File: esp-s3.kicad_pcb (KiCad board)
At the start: 2 copper layers, 12 parts, among them U1 ESP32-S3, U2 W25Q16JVSS

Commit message: 🚀初步完善原理图
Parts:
- added AE2: Antenna_Shield, RF_Antenna:Texas_SWRA117D_2.4GHz_Left, F.Cu at (175.7, 86.2)
- added C10: 10pf, Capacitor_SMD:C_0402_1005Metric, F.Cu at (99.9, 105.7)
- added C11: 10pf, Capacitor_SMD:C_0402_1005Metric, F.Cu at (99.9, 107.7)
- added C12: 1uf, Capacitor_SMD:C_0402_1005Metric, F.Cu at (99.9, 109.6)
- added C13: 10uf, Capacitor_SMD:C_0402_1005Metric, F.Cu at (99.9, 111.6)
- added C14: 1uf, Capacitor_SMD:C_0402_1005Metric, F.Cu at (99.9, 113.6)
- added C15: 10uf, Capacitor_SMD:C_0402_1005Metric, F.Cu at (102.8, 105.7)
- added C16: 100nf, Capacitor_SMD:C_0402_1005Metric, F.Cu at (102.8, 107.7)
- added C17: 1uf, Capacitor_SMD:C_0402_1005Metric, F.Cu at (102.8, 109.6)
- added C18: 15pf, Capacitor_SMD:C_0402_1005Metric, F.Cu at (102.8, 111.6)
- added C19: 15pf, Capacitor_SMD:C_0402_1005Metric, F.Cu at (102.8, 113.6)
- added C20: 4.7PF, Capacitor_SMD:C_0402_1005Metric, F.Cu at (160.5, 86.5)
- added C21: 2.4pf, Capacitor_SMD:C_0402_1005Metric, F.Cu at (159.8, 88.9)
- added D1: NCD0603R1, LED_SMD:LED_0603_1608Metric, F.Cu at (109.6, 96.5)
- added D2: NCD0603R1, LED_SMD:LED_0603_1608Metric, F.Cu at (144.5, 101.6)
- added J1: USB1, Connector_USB:USB_C_Receptacle_G-Switch_GT-USB-7010ASV, F.Cu at (179.6, 133.2)
- added J2: USB1, Connector_USB:USB_C_Receptacle_G-Switch_GT-USB-7010ASV, F.Cu at (165.9, 132.4)
- added L2: 2.4nh, Inductor_SMD:L_0402_1005Metric, F.Cu at (162.6, 90.6)
- added R1: 100Ω, Resistor_SMD:R_0402_1005Metric, F.Cu at (99.9, 91.8)
- added R2: 4.7kΩ, Resistor_SMD:R_0402_1005Metric, F.Cu at (99.9, 93.8)
- added R3: 5.1K, Resistor_SMD:R_0402_1005Metric, F.Cu at (99.9, 95.8)
- added R4: 4.7kΩ, Resistor_SMD:R_0402_1005Metric, F.Cu at (99.9, 97.8)
- added R5: 5.1K, Resistor_SMD:R_0402_1005Metric, F.Cu at (99.9, 99.7)
- added R6: 5.1K, Resistor_SMD:R_0402_1005Metric, F.Cu at (99.9, 101.7)
- added R7: 5.1K, Resistor_SMD:R_0402_1005Metric, F.Cu at (99.9, 103.7)
- added R8: 100Ω, Resistor_SMD:R_0402_1005Metric, F.Cu at (143.9, 103.8)
- added SW1: SW_Push, SmartLock:SW-SMD_L3.9-W3.0-P4.45, F.Cu at (107.5, 106.8)
- added SW3: SW_Push, SmartLock:SW-SMD_L3.9-W3.0-P4.45, F.Cu at (107.5, 111.1)
- added U3: ME6231A33PG, Package_TO_SOT_SMD:SOT-89-3, F.Cu at (104.8, 98.3)
- added U4: CH343P, Package_DFN_QFN:WCH_QFN-16-1EP_3x3mm_P0.5mm_EP1.8x1.8mm, F.Cu at (89.4, 113.6)
- added Y1: Crystal_GND24, Crystal:Crystal_SMD_3225-4Pin_3.2x2.5mm, F.Cu at (178.7, 101.3)
- added Y2: Crystal, SmartLock:Crystal_SMD_ECS_CSM3X-2Pin_7.5x3.1mm, F.Cu at (164.8, 108.3)
- moved U2 55.8 mm to (176.9, 111.0)
- moved U1 51.2 mm to (170.6, 97.9), turned to -90 degrees
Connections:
- C1 pad 1: VDD33 -> VDDSPI
- C2 pad 1: VDD33 -> VDDSPI
- C4 pad 1: VDD33 -> VDDSPI
- C5 pad 1: VDD33 -> VDDSPI
- C6 pad 1: VDD33 -> VDDSPI
- C7 pad 1: VDD33 -> VDDSPI
- C8 pad 1: VDD33 -> VDDSPI
- C9 pad 1: VDD33 -> VDDSPI
- L1 pad 2: VDD33 -> VDDSPI
- U1 pad 1: unconnected-(U1-LNA_IN-Pad1) -> LNA_IN
- U1 pad 10: unconnected-(U1-GPIO5-Pad10) -> GPIO5
- U1 pad 11: unconnected-(U1-GPIO6-Pad11) -> GPIO6
- U1 pad 12: unconnected-(U1-GPIO7-Pad12) -> GPIO7
- U1 pad 13: unconnected-(U1-GPIO8-Pad13) -> GPIO8
- U1 pad 14: unconnected-(U1-GPIO9-Pad14) -> GPIO9
- U1 pad 15: unconnected-(U1-GPIO10-Pad15) -> GPIO10
- U1 pad 16: unconnected-(U1-GPIO11-Pad16) -> GPIO11
- U1 pad 17: unconnected-(U1-GPIO12-Pad17) -> GPIO12
- U1 pad 18: unconnected-(U1-GPIO13-Pad18) -> GPIO13
- U1 pad 19: unconnected-(U1-GPIO14-Pad19) -> GPIO14
- U1 pad 21: unconnected-(U1-XTAL_32K_P-Pad21) -> RTC_P
- U1 pad 22: unconnected-(U1-XTAL_32K_N-Pad22) -> RTC_N
- U1 pad 23: unconnected-(U1-GPIO17-Pad23) -> GPIO17
- U1 pad 24: unconnected-(U1-GPIO18-Pad24) -> GPIO18
- U1 pad 25: unconnected-(U1-GPIO19/USB_D--Pad25) -> USB_D-
- U1 pad 26: unconnected-(U1-GPIO20/USB_D+-Pad26) -> USB_D+
- U1 pad 27: unconnected-(U1-GPIO21-Pad27) -> GPIO21
- U1 pad 29: VDD33 -> VDDSPI
- U1 pad 30: unconnected-(U1-SPIHD-Pad30) -> SPIHD
- U1 pad 31: unconnected-(U1-SPIWP-Pad31) -> SPIWP
- U1 pad 33: unconnected-(U1-SPICLK-Pad33) -> SPICLK
- U1 pad 34: unconnected-(U1-SPIQ-Pad34) -> SPIQ
- U1 pad 35: unconnected-(U1-SPID-Pad35) -> SPID
- U1 pad 36: unconnected-(U1-SPICLK_N-Pad36) -> GPIO48
- U1 pad 37: unconnected-(U1-SPICLK_P-Pad37) -> GPIO47
- U1 pad 38: unconnected-(U1-GPIO33-Pad38) -> GPIO33
- U1 pad 39: unconnected-(U1-GPIO34-Pad39) -> GPIO34
- U1 pad 4: unconnected-(U1-CHIP_PU-Pad4) -> CHIP_PU
- U1 pad 40: unconnected-(U1-GPIO35-Pad40) -> GPIO35
- U1 pad 41: unconnected-(U1-GPIO36-Pad41) -> GPIO36
- U1 pad 42: unconnected-(U1-GPIO37-Pad42) -> GPIO37
- U1 pad 43: unconnected-(U1-GPIO38-Pad43) -> GPIO38
- U1 pad 44: unconnected-(U1-MTCK-Pad44) -> GPIO39
- U1 pad 45: unconnected-(U1-MTDO-Pad45) -> GPIO40
- U1 pad 46: VDD33 -> VDDSPI
- U1 pad 47: unconnected-(U1-MTDI-Pad47) -> GPIO41
- U1 pad 48: unconnected-(U1-MTMS-Pad48) -> GPIO42
- U1 pad 49: unconnected-(U1-U0TXD-Pad49) -> TXD
- U1 pad 5: unconnected-(U1-GPIO0-Pad5) -> GPIO0
- U1 pad 50: unconnected-(U1-U0RXD-Pad50) -> RXD
- U1 pad 51: unconnected-(U1-GPIO45-Pad51) -> GPIO45
- U1 pad 52: unconnected-(U1-GPIO46-Pad52) -> GPIO46
- U1 pad 53: unconnected-(U1-XTAL_N-Pad53) -> XTAL_N
- U1 pad 54: unconnected-(U1-XTAL_P-Pad54) -> XTAL_P
- U1 pad 55: VDD33 -> VDDSPI
- U1 pad 56: VDD33 -> VDDSPI
- U1 pad 6: unconnected-(U1-GPIO1-Pad6) -> GPIO1
- U1 pad 7: unconnected-(U1-GPIO2-Pad7) -> GPIO2
- U1 pad 8: unconnected-(U1-GPIO3-Pad8) -> GPIO3
- U1 pad 9: unconnected-(U1-GPIO4-Pad9) -> GPIO4
- U2 pad 2: unconnected-(U2-DO/IO_{1}-Pad2) -> SPIQ
- U2 pad 3: unconnected-(U2-~{WP}/IO_{2}-Pad3) -> SPIWP
- U2 pad 4: unconnected-(U2-GND-Pad4) -> GND
- U2 pad 5: unconnected-(U2-DI/IO_{0}-Pad5) -> SPID
- U2 pad 6: unconnected-(U2-CLK-Pad6) -> SPICLK
- U2 pad 7: unconnected-(U2-~{HOLD}/~{RESET}/IO_{3}-Pad7) -> SPIHD
- U2 pad 8: unconnected-(U2-VCC-Pad8) -> VDDSPI
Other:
- board outline added: 30.7 x 56.6 mm

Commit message: 初步完成PCB
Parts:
- removed C18, C19: 15pf, Capacitor_SMD:C_0402_1005Metric
- removed Y2: Crystal, SmartLock:Crystal_SMD_ECS_CSM3X-2Pin_7.5x3.1mm
- added C22: 100nf, Capacitor_SMD:C_0402_1005Metric, F.Cu at (166.9, 94.3)
- added J3: Conn_01x15_Pin, Connector_PinHeader_2.54mm:PinHeader_1x20_P2.54mm_Vertical, F.Cu at (156.6, 80.3)
- added J4: Conn_01x15_Pin, Connector_PinHeader_2.54mm:PinHeader_1x20_P2.54mm_Vertical, F.Cu at (185.6, 80.0)
- SW1, SW3: footprint SmartLock:SW-SMD_L3.9-W3.0-P4.45 -> smartlock:SW-SMD_L3.9-W3.0-P4.45
- moved U4 88.4 mm to (177.8, 115.4)
- moved R5 82.5 mm to (180.1, 119.1), turned to -90 degrees
- moved R1 82.2 mm to (179.7, 111.5)
- moved R3 80.3 mm to (176.8, 118.9)
- moved C11 78.5 mm to (177.4, 95.0), turned to -90 degrees
- moved C10 78.5 mm to (177.4, 93.2), turned to 90 degrees
- moved C16 74.7 mm to (176.8, 118.0)
- moved C17 72.7 mm to (175.4, 113.3), turned to -90 degrees
- moved C14 72.7 mm to (168.2, 88.6), turned to 90 degrees
- moved C15 72.5 mm to (174.2, 118.1), turned to -90 degrees
- moved D1 71.4 mm to (179.7, 109.5), turned to -90 degrees
- moved C13 71.3 mm to (170.9, 118.5), turned to 180 degrees
- moved R7 70.1 mm to (168.3, 119.0), turned to -90 degrees
- moved C12 70.0 mm to (166.8, 88.7), turned to 90 degrees
- moved U3 68.6 mm to (171.2, 115.2), turned to 90 degrees
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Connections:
- C1 pad 1: VDDSPI -> VDD33
- C12 pad 1: Net-(C12-Pad1) -> GPIO0
- C14 pad 1: Net-(C14-Pad1) -> CHIP_PU
- C15 pad 1: VDDSPI -> VDD33
- C17 pad 2: VDDSPI -> VDD33
- C2 pad 1: VDDSPI -> VDD33
- C4 pad 1: VDDSPI -> VDD33
- C5 pad 1: VDDSPI -> VDD33
- C6 pad 1: VDDSPI -> VDD33
- C7 pad 1: VDDSPI -> VDD33
- D1 pad 1: GPIO2 -> GPIO39
- L1 pad 2: VDDSPI -> VDD33
- R1 pad 1: VDDSPI -> VDD33
- R2 pad 1: Net-(C12-Pad1) -> GPIO0
- R2 pad 2: VDDSPI -> VDD33
- R4 pad 1: Net-(C14-Pad1) -> CHIP_PU
- R4 pad 2: VDDSPI -> VDD33
- R8 pad 1: VDDSPI -> VDD33
- SW1 pad 1: Net-(C12-Pad1) -> GND
- SW3 pad 1: Net-(C14-Pad1) -> GND
- U1 pad 20: unconnected-(U1-VDD3P3_RTC-Pad20) -> VDD33
- U1 pad 21: RTC_P -> GPIO15
- U1 pad 22: RTC_N -> GPIO16
- U1 pad 46: VDDSPI -> VDD33
- U1 pad 55: VDDSPI -> VDD33
- U1 pad 56: VDDSPI -> VDD33
- U3 pad 3: VDDSPI -> VDD33
- U4 pad 1: VDDSPI -> VDD33
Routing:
- net VDD33: track 0.00 -> 132.3 mm, vias 0 -> 10
- net CHIP_PU: track 0.00 -> 62.3 mm, vias 0 -> 5
- net GPIO0: track 0.00 -> 58.6 mm, vias 0 -> 5
- net VBUS: track 0.00 -> 39.7 mm, vias 0 -> 6
- net GPIO18: track 0.00 -> 39.5 mm, vias 0 -> 2
- net GPIO48: track 0.00 -> 39.1 mm, vias 0 -> 1
- net GPIO21: track 0.00 -> 38.4 mm, vias 0 -> 1
- net GPIO47: track 0.00 -> 36.7 mm, vias 0 -> 1
- net GPIO17: track 0.00 -> 36.5 mm
- net GPIO16: track 0.00 -> 34.4 mm
- net GPIO33: track 0.00 -> 34.4 mm, vias 0 -> 1
- net USB_D-: track 0.00 -> 31.9 mm
- net GPIO39: track 0.00 -> 31.6 mm, vias 0 -> 2
- net GPIO34: track 0.00 -> 31.5 mm, vias 0 -> 1
- net GPIO15: track 0.00 -> 31.5 mm
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- added copper zone on B.Cu, net GND
- added copper zone on F.Cu, net GND
- added copper zone on In1.Cu, net GND
- added copper zone on In2.Cu, net GND
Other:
- board size 30.7 x 56.6 mm -> 32.4 x 51.6 mm
- copper layers 2 -> 4

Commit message: 添加pcb丝印
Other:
- board text added: "GND"
- board text added: "GPIO1"
- board text added: "GPIO10"
- board text added: "GPIO11"
- board text added: "GPIO12"
- board text added: "GPIO13"
- board text added: "GPIO14"
- board text added: "GPIO15"
- board text added: "GPIO16"
- board text added: "GPIO17"
- board text added: "GPIO18"
- board text added: "GPIO2"
- board text added: "GPIO21"
- board text added: "GPIO3"
- board text added: "GPIO33"
- board text added: "GPIO34"
- board text added: "GPIO35"
- board text added: "GPIO36"
- board text added: "GPIO37"
- board text added: "GPIO38"
- board text added: "GPIO39"
- board text added: "GPIO4"
- board text added: "GPIO40"
- board text added: "GPIO41"
- board text added: "GPIO42"
- board text added: "GPIO45"
- board text added: "GPIO46"
- board text added: "GPIO47"
- board text added: "GPIO48"
- board text added: "GPIO5"
- board text added: "GPIO6"
- board text added: "GPIO7"
- board text added: "GPIO8"
- board text added: "GPIO9"
- board text added: "VDD33"

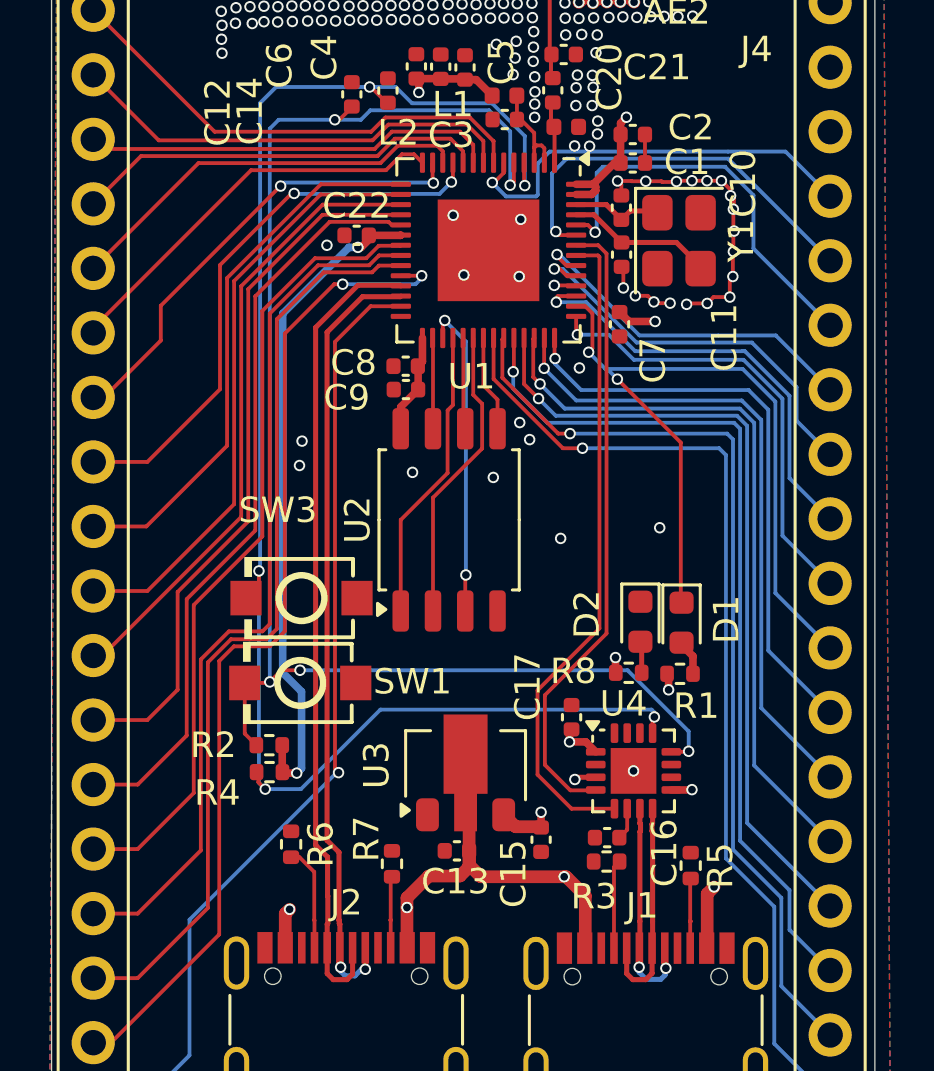
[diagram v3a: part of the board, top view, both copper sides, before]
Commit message: 丝印修改
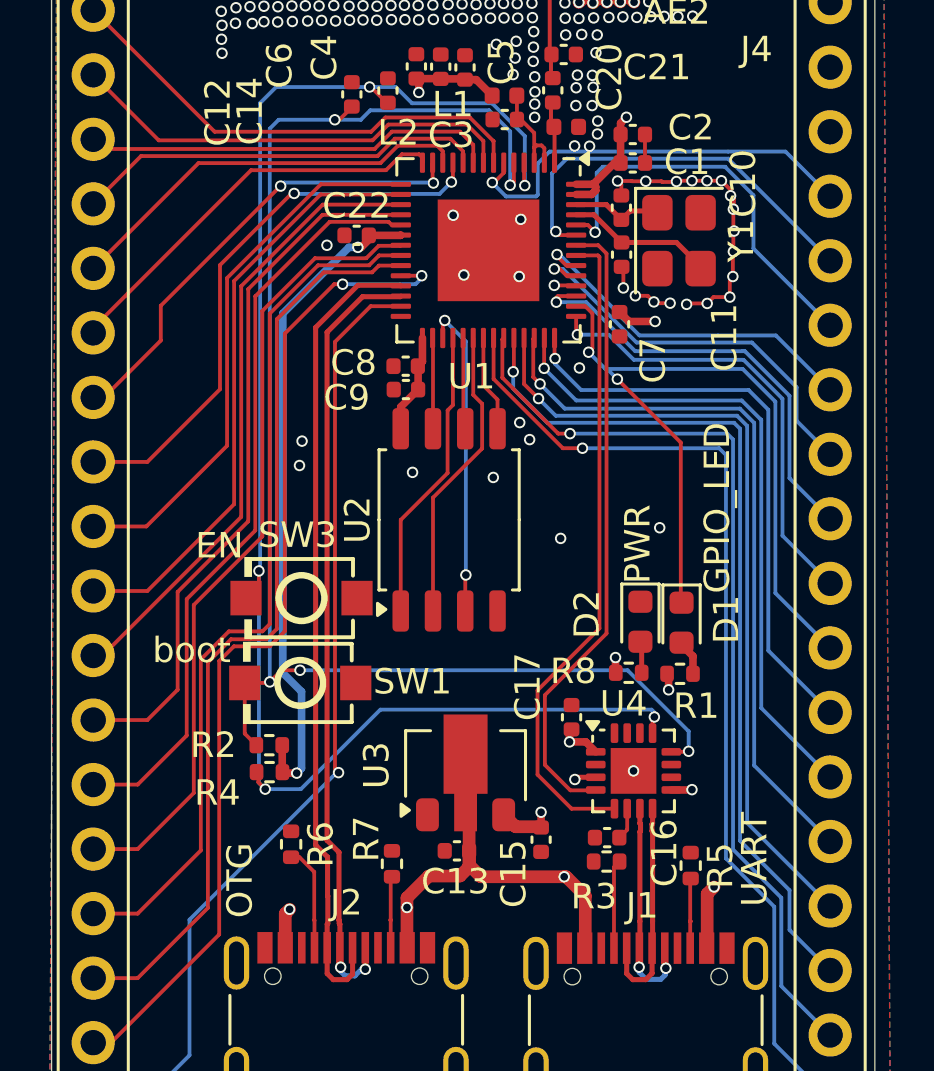
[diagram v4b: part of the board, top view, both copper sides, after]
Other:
- board text added: "EN"
- board text added: "GPIO_LED"
- board text added: "OTG"
- board text added: "PWR"
- board text added: "UART"
- board text added: "boot"
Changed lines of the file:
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@@
 		(at 164.77 108.57 180)
 		(property "Reference" "SW3"
-			(at 0.93 3.46 180)
+			(at 0.16 2.48 180)
 			(layer "F.SilkS")
 			(effects
@@
 		(layer "Edge.Cuts")
 	)
+	(gr_text "UART"
+		(at 183.19 120.72 90)
+		(layer "F.SilkS" knockout)
+		(effects
+			(font
+				(size 1 1)
+				(thickness 0.1)
+			)
+			(justify left bottom)
+		)
+	)
+	(gr_text "PWR"
+		(at 178.59 108.015 90)
+		(layer "F.SilkS" knockout)
+		(effects
+			(font
+				(size 1 1)
+				(thickness 0.1)
+			)
+			(justify left bottom)
+		)
+	)
+	(gr_text "boot\n"
+		(at 158.9 111.21 0)
+		(layer "F.SilkS" knockout)
+		(effects
+			(font
+				(size 1 1)
+				(thickness 0.1)
+			)
+			(justify left bottom)
+		)
+	)
+	(gr_text "GPIO_LED\n"
+		(at 181.72 108.39 90)
+		(layer "F.SilkS" knockout)
+		(effects
+			(font
+				(size 1 1)
+				(thickness 0.1)
+			)
+			(justify left bottom)
+		)
+	)
+	(gr_text "EN"
+		(at 160.59 107.09 0)
+		(layer "F.SilkS" knockout)
+		(effects
+			(font
+				(size 1 1)
+				(thickness 0.1)
+			)
+			(justify left bottom)
+		)
+	)
+	(gr_text "OTG"
+		(at 162.93 121.17 90)
+		(layer "F.SilkS" knockout)
+		(effects
+			(font
+				(size 1 1)
+				(thickness 0.1)
+			)
+			(justify left bottom)
+		)
+	)
 	(gr_text "GPIO47"
 		(at 184.03 125.75 0)
@@
 	)
 	(segment
-		(start 169.53 91.43)
-		(end 169.2 91.1)
+		(start 162.786 91.724)
+		(end 156.57 97.94)
 		(width 0.15)
 		(layer "F.Cu")
@@
 	)
 	(segment
-		(start 168.096 91.724)
-		(end 162.786 91.724)
+		(start 168.72 91.1)
+		(end 168.096 91.724)
 		(width 0.15)
 		(layer "F.Cu")
@@
 	)
 	(segment
-		(start 168.72 91.1)
-		(end 168.096 91.724)
+		(start 156.57 97.94)
+		(end 156.57 98.13)
 		(width 0.15)
 		(layer "F.Cu")
@@
 	)
 	(segment
-		(start 162.786 91.724)
-		(end 156.57 97.94)
+		(start 169.53 91.23)
+		(end 169.4 91.1)
 		(width 0.15)
 		(layer "F.Cu")
@@
 	)
 	(segment
-		(start 156.57 97.94)
-		(end 156.57 98.13)
+		(start 169.53 91.43)
+		(end 169.53 91.23)
 		(width 0.15)
 		(layer "F.Cu")
@@
 	)
 	(segment
-		(start 169.2 91.1)
+		(start 169.4 91.1)
 		(end 168.72 91.1)
 		(width 0.15)
 		(layer "F.Cu")
+		(net 38)
+	)
+	(segment
+		(start 168.096 91.724)
+		(end 162.786 91.724)
+		(width 0.15)
+		(layer "F.Cu")

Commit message: 修复L3电源层
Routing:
- net VDD33: track 132.3 -> 42.8 mm
- net GND: track 19.7 -> 14.5 mm, vias 123 -> 99
- added copper zone on In2.Cu, net VDD33
- removed copper zone on In2.Cu, net GND
